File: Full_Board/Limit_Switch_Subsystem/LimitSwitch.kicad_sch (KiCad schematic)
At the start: 7 parts, among them J11 OQ0212500000G, U12 UCLAMP3301H.TCT

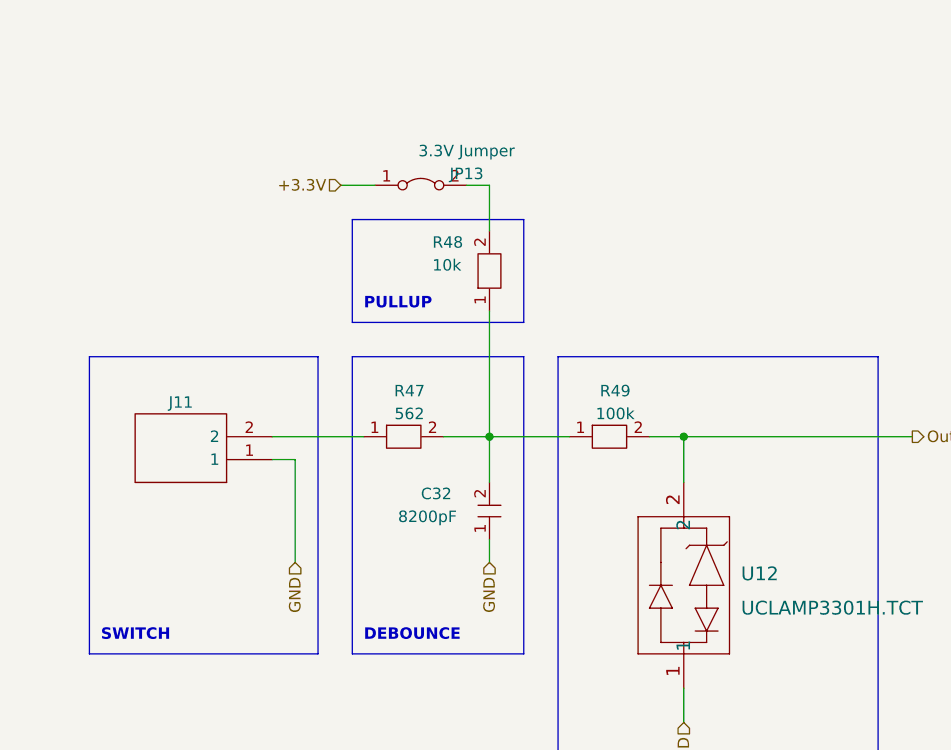
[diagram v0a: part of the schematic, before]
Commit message: Merge GND planes, update gitignore rules
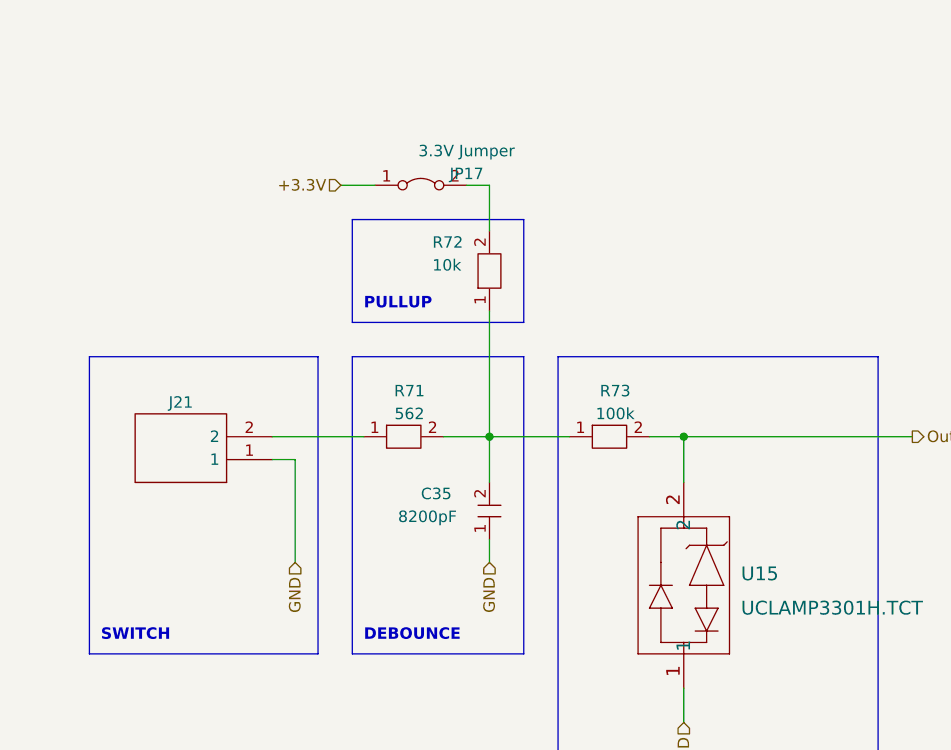
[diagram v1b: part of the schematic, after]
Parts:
- renumbered C32 to C35, J11 to J21, JP13 to JP17, R47 to R71, R48 to R72, R49 to R73, U12 to U15
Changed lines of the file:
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@@
   (symbol (lib_id "OQ0212500000G:OQ0212500000G") (at 119.38 92.71 180) (unit 1)
     (in_bom yes) (on_board yes)
-    (property "Reference" "J11" (id 0) (at 109.22 86.36 0))
+    (property "Reference" "J21" (id 0) (at 109.22 86.36 0))
     (property "Value" "OQ0212500000G" (id 1) (at 109.22 85.09 0)
       (effects (font (size 1.27 1.27)) hide)
@@
   (symbol (lib_id "CR0402-FX-5620GLF:CR0402-FX-5620GLF") (at 129.54 90.17 0) (unit 1)
     (in_bom yes) (on_board yes)
-    (property "Reference" "R47" (id 0) (at 134.62 85.09 0))
+    (property "Reference" "R71" (id 0) (at 134.62 85.09 0))
     (property "Value" "562" (id 1) (at 134.62 87.63 0))
     (property "Footprint" "CR0402-FX-5620GLF:RESC1005X40N" (id 2) (at 143.51 88.9 0)
@@
   (symbol (lib_id "RMCF1206FT10K0:10k") (at 143.51 76.2 90) (unit 1)
     (in_bom yes) (on_board yes)
-    (property "Reference" "R48" (id 0) (at 137.16 68.58 90)
+    (property "Reference" "R72" (id 0) (at 137.16 68.58 90)
       (effects (font (size 1.27 1.27)) (justify right))
     )
@@
   (symbol (lib_id "RCV2512100KFKEGAT:RCV2512100KFKEGAT") (at 152.4 90.17 0) (unit 1)
     (in_bom yes) (on_board yes)
-    (property "Reference" "R49" (id 0) (at 157.48 85.09 0))
+    (property "Reference" "R73" (id 0) (at 157.48 85.09 0))
     (property "Value" "100k" (id 1) (at 157.48 87.63 0))
     (property "Footprint" "RCV2512100KFKEGAT:RESC6332X70N" (id 2) (at 166.37 88.9 0)
@@
   (symbol (lib_id "C1210C822K2RACAUTO:C1210C822K2RACAUTO") (at 143.51 101.6 90) (unit 1)
     (in_bom yes) (on_board yes)
-    (property "Reference" "C32" (id 0) (at 135.89 96.52 90)
+    (property "Reference" "C35" (id 0) (at 135.89 96.52 90)
       (effects (font (size 1.27 1.27)) (justify right))
     )
@@
   (symbol (lib_id "Jumper:Jumper_2_Bridged") (at 135.89 62.23 0) (unit 1)
     (in_bom yes) (on_board yes)
-    (property "Reference" "JP13" (id 0) (at 140.97 60.96 0))
+    (property "Reference" "JP17" (id 0) (at 140.97 60.96 0))
     (property "Value" "3.3V Jumper" (id 1) (at 140.97 58.42 0))
     (property "Footprint" "TestPoint:TestPoint_2Pads_Pitch2.54mm_Drill0.8mm" (id 2) (at 135.89 62.23 0)
@@
   (symbol (lib_id "UCLAMP3301H-TCT:UCLAMP3301H.TCT") (at 165.1 127 90) (unit 1)
     (in_bom yes) (on_board yes) (fields_autoplaced)
-    (property "Reference" "U12" (id 0) (at 171.45 105.41 90)
+    (property "Reference" "U15" (id 0) (at 171.45 105.41 90)
       (effects (font (size 1.524 1.524)) (justify right))
     )

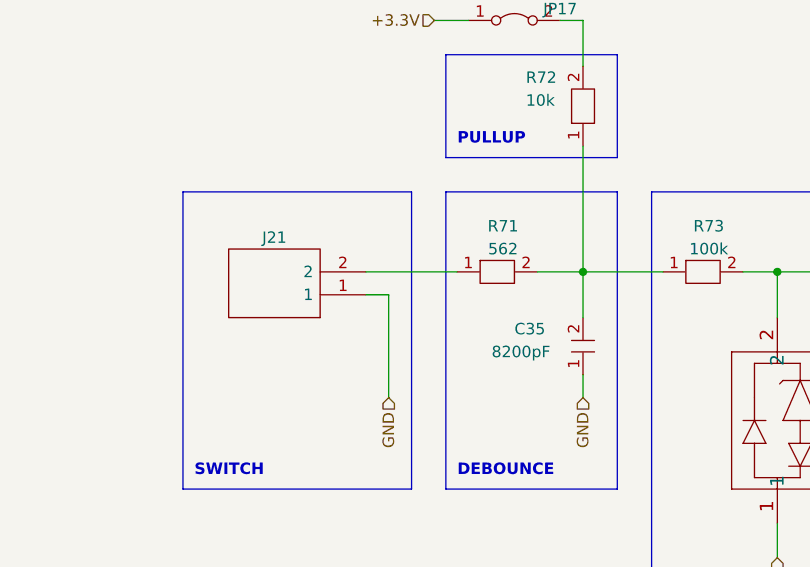
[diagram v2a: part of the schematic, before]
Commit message: Fix vias for Analog Digital's requirements
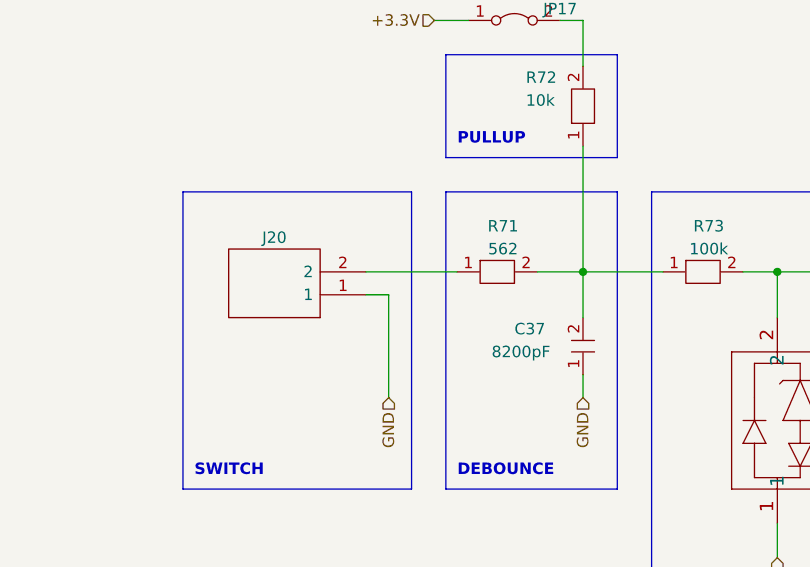
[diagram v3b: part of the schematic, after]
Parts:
- renumbered C35 to C37, J21 to J20
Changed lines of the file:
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@@
   (symbol (lib_id "OQ0212500000G:OQ0212500000G") (at 119.38 92.71 180) (unit 1)
     (in_bom yes) (on_board yes)
-    (property "Reference" "J21" (id 0) (at 109.22 86.36 0))
+    (property "Reference" "J20" (id 0) (at 109.22 86.36 0))
     (property "Value" "OQ0212500000G" (id 1) (at 109.22 85.09 0)
       (effects (font (size 1.27 1.27)) hide)
@@
   (symbol (lib_id "C1210C822K2RACAUTO:C1210C822K2RACAUTO") (at 143.51 101.6 90) (unit 1)
     (in_bom yes) (on_board yes)
-    (property "Reference" "C35" (id 0) (at 135.89 96.52 90)
+    (property "Reference" "C37" (id 0) (at 135.89 96.52 90)
       (effects (font (size 1.27 1.27)) (justify right))
     )

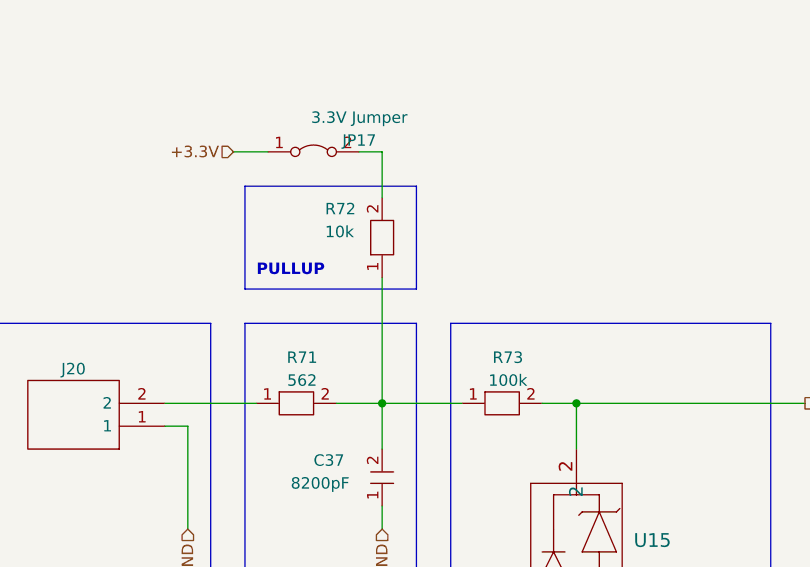
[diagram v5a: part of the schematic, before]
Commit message: Replace small resistors/capacitors with through-hole; fix DRC aside from electromagnet and MUXes
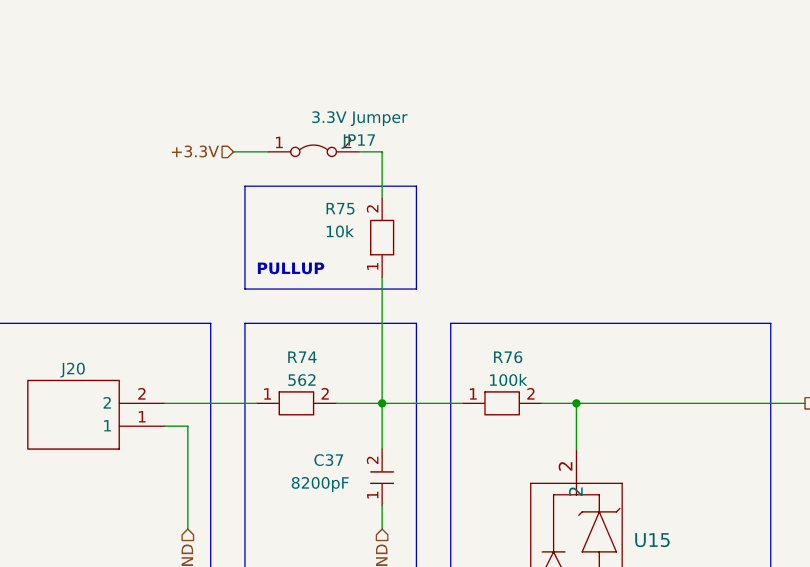
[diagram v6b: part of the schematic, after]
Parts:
- renumbered R71 to R74, R72 to R75, R73 to R76
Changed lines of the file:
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@@
   (symbol (lib_id "CR0402-FX-5620GLF:CR0402-FX-5620GLF") (at 129.54 90.17 0) (unit 1)
     (in_bom yes) (on_board yes)
-    (property "Reference" "R71" (id 0) (at 134.62 85.09 0))
+    (property "Reference" "R74" (id 0) (at 134.62 85.09 0))
     (property "Value" "562" (id 1) (at 134.62 87.63 0))
     (property "Footprint" "CR0402-FX-5620GLF:RESC1005X40N" (id 2) (at 143.51 88.9 0)
@@
   (symbol (lib_id "RMCF1206FT10K0:10k") (at 143.51 76.2 90) (unit 1)
     (in_bom yes) (on_board yes)
-    (property "Reference" "R72" (id 0) (at 137.16 68.58 90)
+    (property "Reference" "R75" (id 0) (at 137.16 68.58 90)
       (effects (font (size 1.27 1.27)) (justify right))
     )
@@
   (symbol (lib_id "RCV2512100KFKEGAT:RCV2512100KFKEGAT") (at 152.4 90.17 0) (unit 1)
     (in_bom yes) (on_board yes)
-    (property "Reference" "R73" (id 0) (at 157.48 85.09 0))
+    (property "Reference" "R76" (id 0) (at 157.48 85.09 0))
     (property "Value" "100k" (id 1) (at 157.48 87.63 0))
     (property "Footprint" "RCV2512100KFKEGAT:RESC6332X70N" (id 2) (at 166.37 88.9 0)

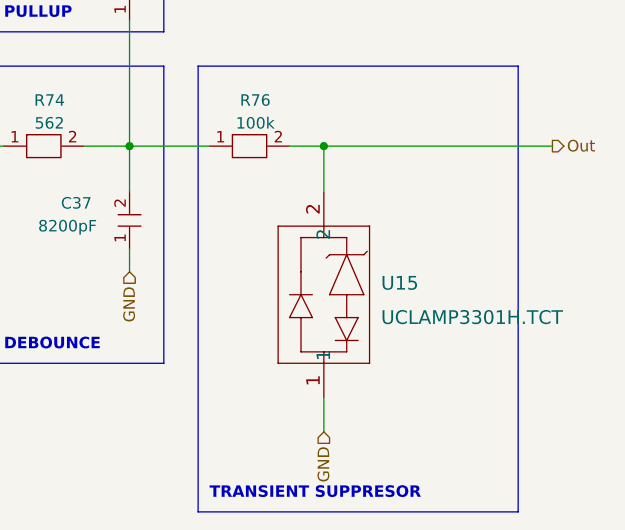
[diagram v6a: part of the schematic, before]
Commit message: Replace MUX/DEMUX; DRC passes aside from electromagnet
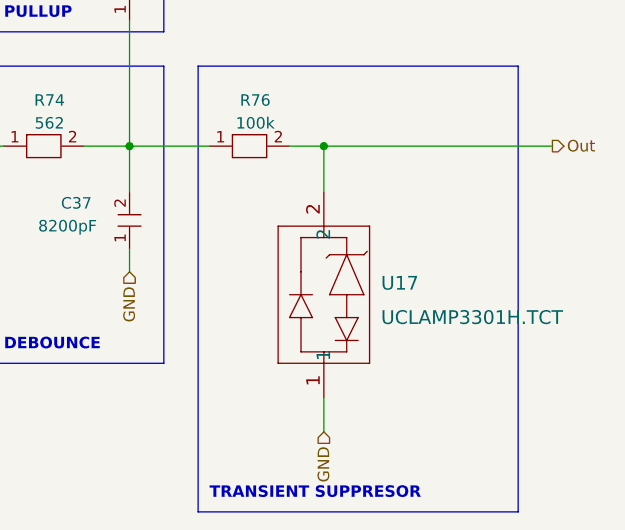
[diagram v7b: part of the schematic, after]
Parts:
- renumbered U15 to U17
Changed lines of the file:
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@@
   (symbol (lib_id "UCLAMP3301H-TCT:UCLAMP3301H.TCT") (at 165.1 127 90) (unit 1)
     (in_bom yes) (on_board yes) (fields_autoplaced)
-    (property "Reference" "U15" (id 0) (at 171.45 105.41 90)
+    (property "Reference" "U17" (id 0) (at 171.45 105.41 90)
       (effects (font (size 1.524 1.524)) (justify right))
     )
